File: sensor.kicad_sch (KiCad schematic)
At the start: 7 parts, among them U1 MAXM86161EFD+T

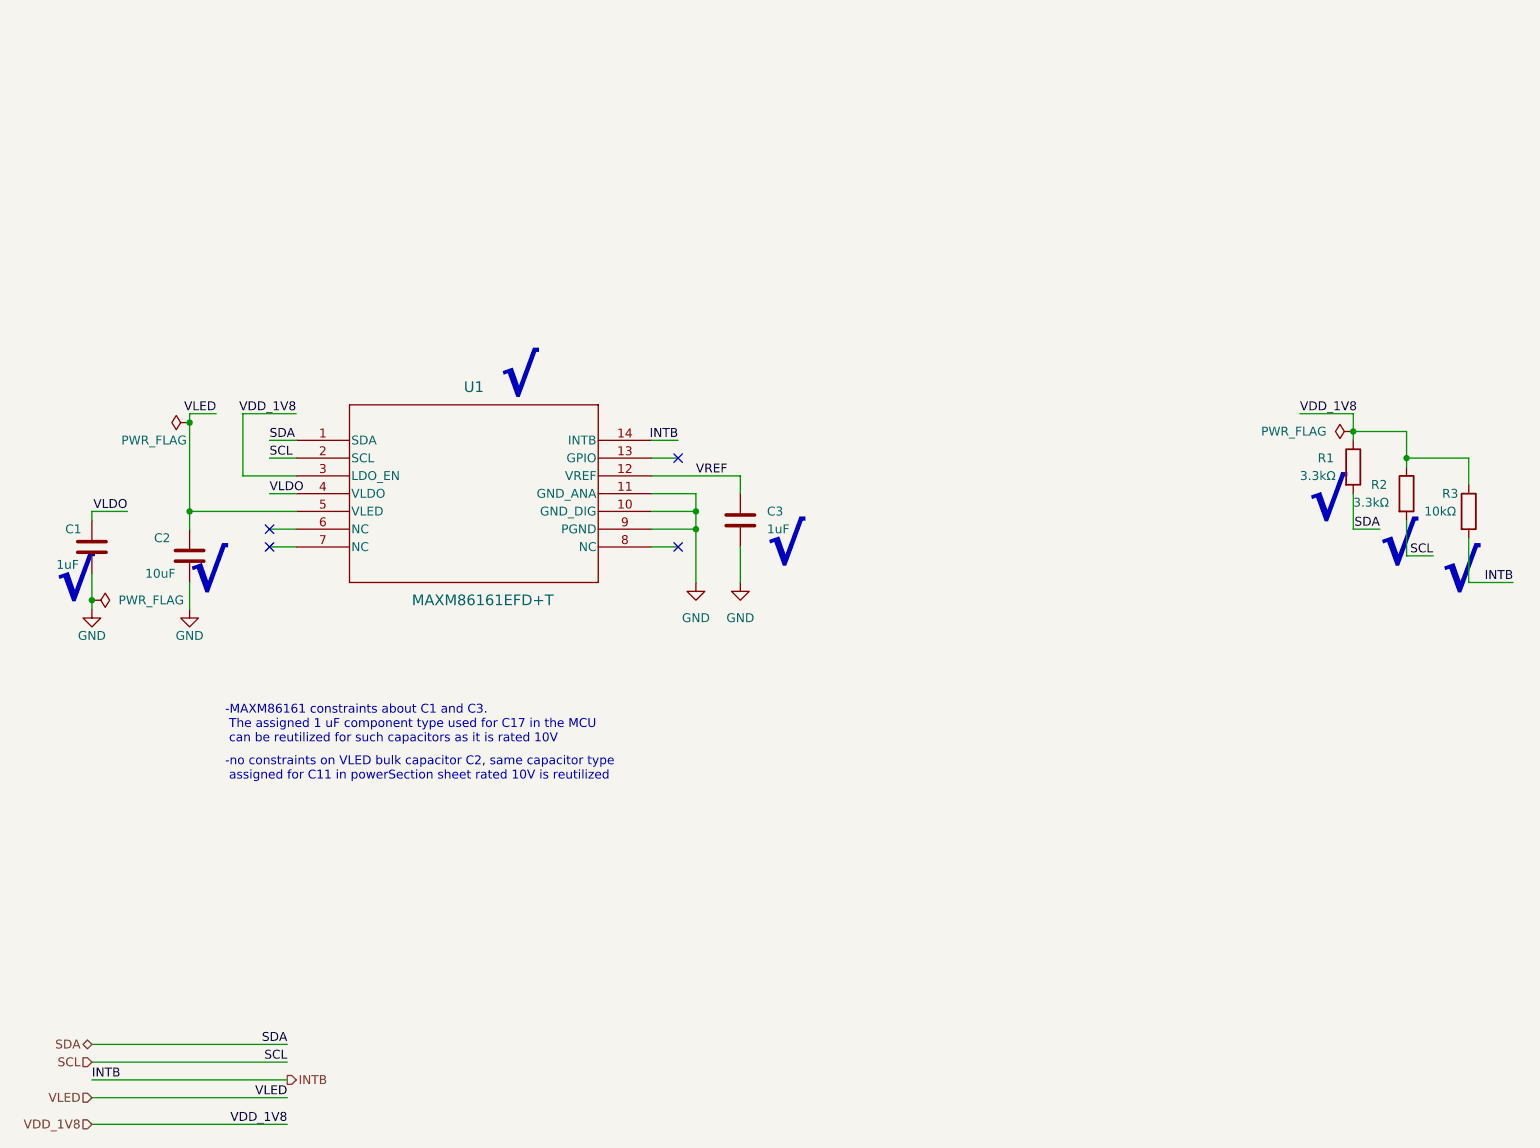
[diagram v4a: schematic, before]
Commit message: finished layout, associated 3d models for the components, drc ran with no errors. fixed foorprints and their individaul pad dimensions (solder mask layer related, copper layer related and paste mask layer related) . EUROCIRCUITS Manufacturer report resulted in class 4C , standard and towards low cost. still needs to fix and revise silkscreen and fabrication layer
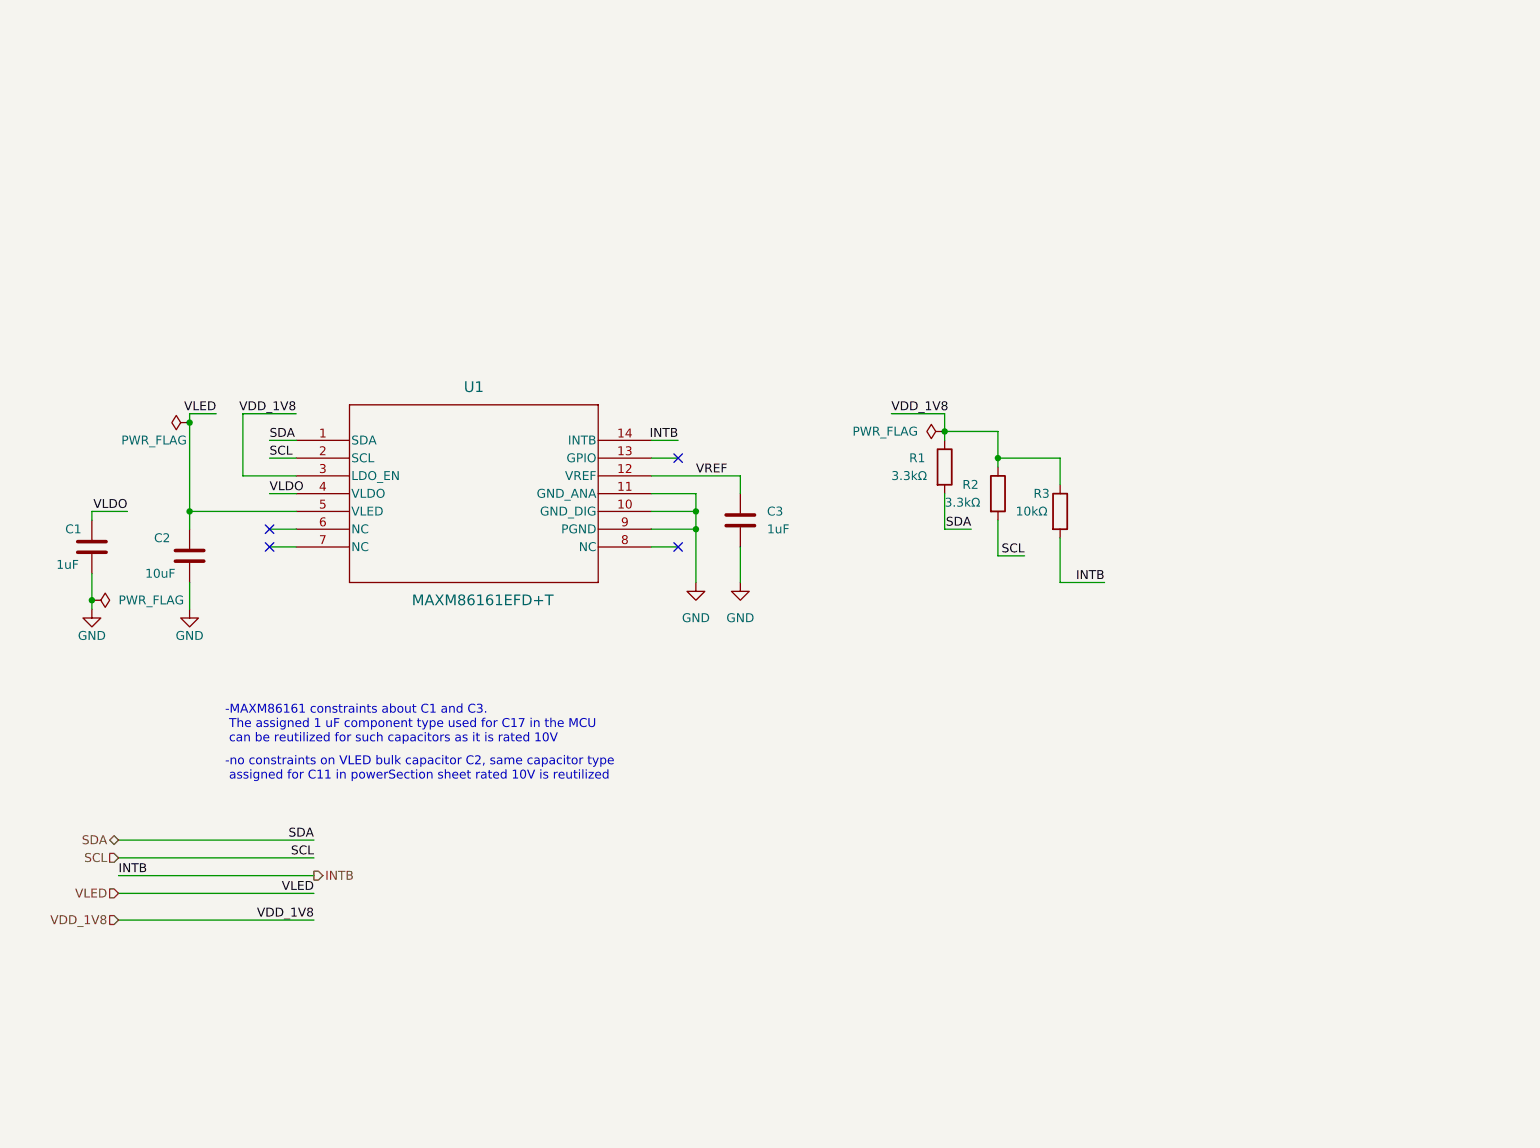
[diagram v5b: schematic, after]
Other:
- note removed: "√"
- moved on the sheet: R1, R2, R3
